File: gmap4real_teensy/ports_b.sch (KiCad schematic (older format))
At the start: 12 parts

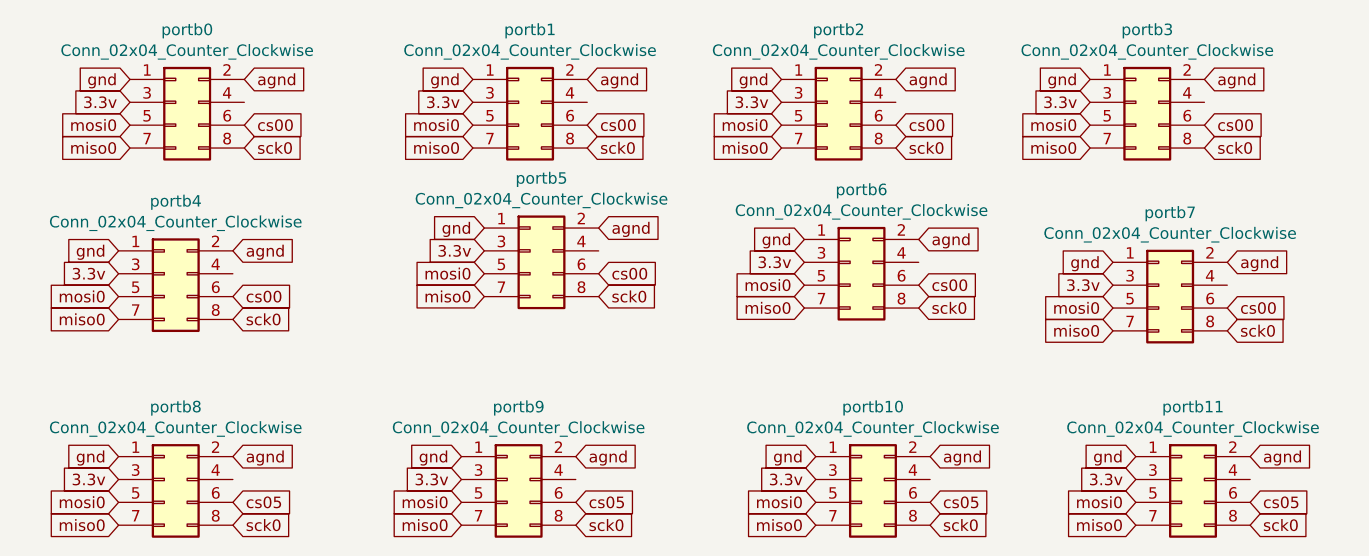
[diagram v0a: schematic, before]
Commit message: teensy: fix select pin conflict
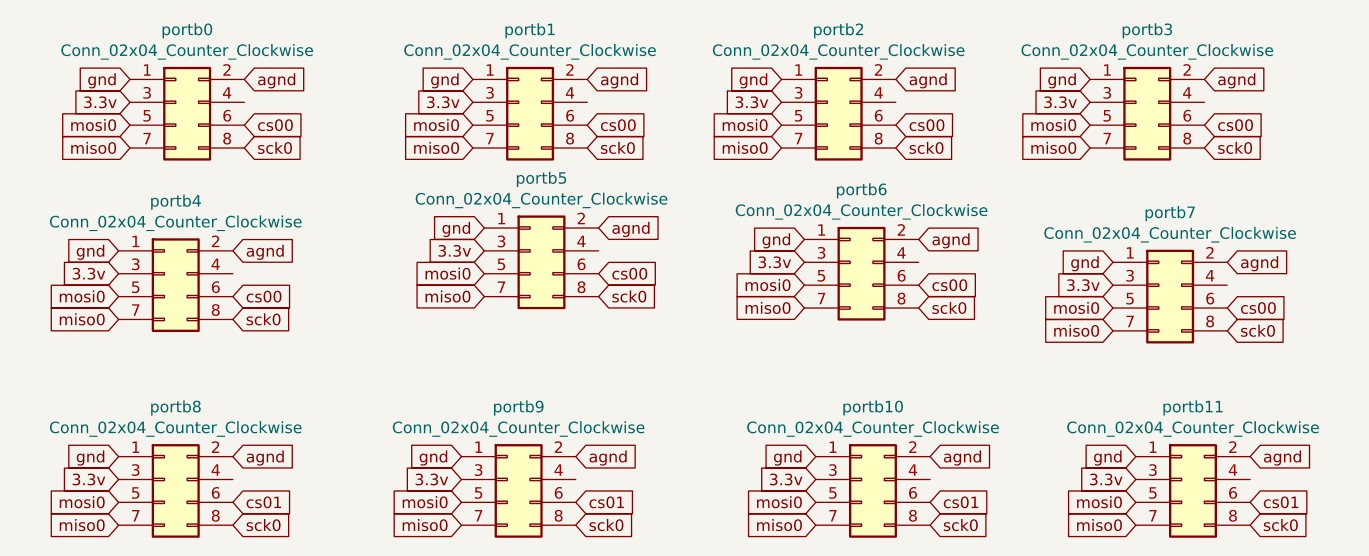
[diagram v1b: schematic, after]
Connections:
- net cs05 renamed cs01
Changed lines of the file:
@@
 agnd
 Text GLabel 2750 4050 2    50   Input ~ 0
-cs05
+cs01
 $Comp
 L Connector_Generic:Conn_02x04_Odd_Even portb9
@@
 agnd
 Text GLabel 4250 4050 2    50   Input ~ 0
-cs05
+cs01
 $Comp
 L Connector_Generic:Conn_02x04_Odd_Even portb10
@@
 agnd
 Text GLabel 5800 4050 2    50   Input ~ 0
-cs05
+cs01
 $Comp
 L Connector_Generic:Conn_02x04_Odd_Even portb11
@@
 agnd
 Text GLabel 7200 4050 2    50   Input ~ 0
-cs05
+cs01
 $EndSCHEMATC

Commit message: teensy: simplify (no agnd to buttons, no agnd to i2c port)
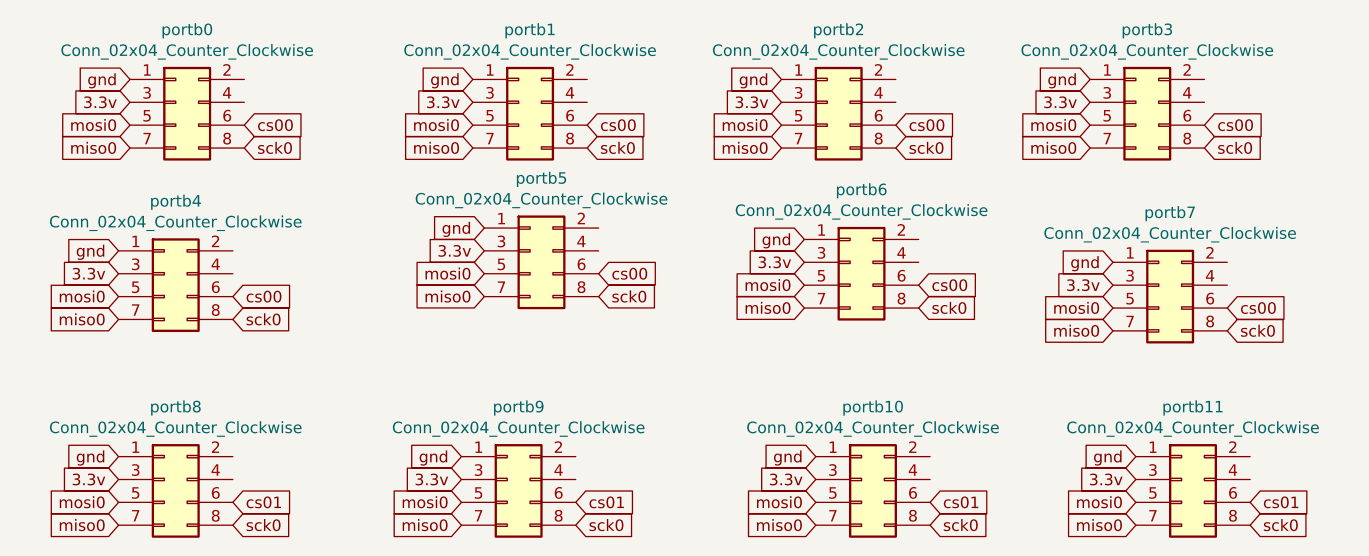
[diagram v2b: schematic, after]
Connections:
- removed net agnd: portb0.2 (Pin_2), portb1.2 (Pin_2), portb10.2 (Pin_2), portb11.2 (Pin_2), portb2.2 (Pin_2), portb3.2 (Pin_2), portb4.2 (Pin_2), portb5.2 (Pin_2), portb6.2 (Pin_2), portb7.2 (Pin_2), portb8.2 (Pin_2), portb9.2 (Pin_2)
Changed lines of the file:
@@
 Text GLabel 2800 2500 2    50   Input ~ 0
 sck0
-Text GLabel 2800 2200 2    50   Input ~ 0
-agnd
 Text GLabel 2800 2400 2    50   Input ~ 0
 cs00
@@
 Text GLabel 4300 2500 2    50   Input ~ 0
 sck0
-Text GLabel 4300 2200 2    50   Input ~ 0
-agnd
 Text GLabel 4300 2400 2    50   Input ~ 0
 cs00
@@
 Text GLabel 5650 2500 2    50   Input ~ 0
 sck0
-Text GLabel 5650 2200 2    50   Input ~ 0
-agnd
 Text GLabel 5650 2400 2    50   Input ~ 0
 cs00
@@
 Text GLabel 7000 2500 2    50   Input ~ 0
 sck0
-Text GLabel 7000 2200 2    50   Input ~ 0
-agnd
 Text GLabel 7000 2400 2    50   Input ~ 0
 cs00
@@
 Text GLabel 2750 3250 2    50   Input ~ 0
 sck0
-Text GLabel 2750 2950 2    50   Input ~ 0
-agnd
 Text GLabel 2750 3150 2    50   Input ~ 0
 cs00
@@
 Text GLabel 4350 3150 2    50   Input ~ 0
 sck0
-Text GLabel 4350 2850 2    50   Input ~ 0
-agnd
 Text GLabel 4350 3050 2    50   Input ~ 0
 cs00
@@
 Text GLabel 5750 3200 2    50   Input ~ 0
 sck0
-Text GLabel 5750 2900 2    50   Input ~ 0
-agnd
 Text GLabel 5750 3100 2    50   Input ~ 0
 cs00
@@
 Text GLabel 7100 3300 2    50   Input ~ 0
 sck0
-Text GLabel 7100 3000 2    50   Input ~ 0
-agnd
 Text GLabel 7100 3200 2    50   Input ~ 0
 cs00
@@
 Text GLabel 2750 4150 2    50   Input ~ 0
 sck0
-Text GLabel 2750 3850 2    50   Input ~ 0
-agnd
 Text GLabel 2750 4050 2    50   Input ~ 0
 cs01
@@
 Text GLabel 4250 4150 2    50   Input ~ 0
 sck0
-Text GLabel 4250 3850 2    50   Input ~ 0
-agnd
 Text GLabel 4250 4050 2    50   Input ~ 0
 cs01
@@
 Text GLabel 5800 4150 2    50   Input ~ 0
 sck0
-Text GLabel 5800 3850 2    50   Input ~ 0
-agnd
 Text GLabel 5800 4050 2    50   Input ~ 0
 cs01
@@
 Text GLabel 7200 4150 2    50   Input ~ 0
 sck0
-Text GLabel 7200 3850 2    50   Input ~ 0
-agnd
 Text GLabel 7200 4050 2    50   Input ~ 0
 cs01
